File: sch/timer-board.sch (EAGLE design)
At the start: 33 parts, among them IC1 ATMEGA328P

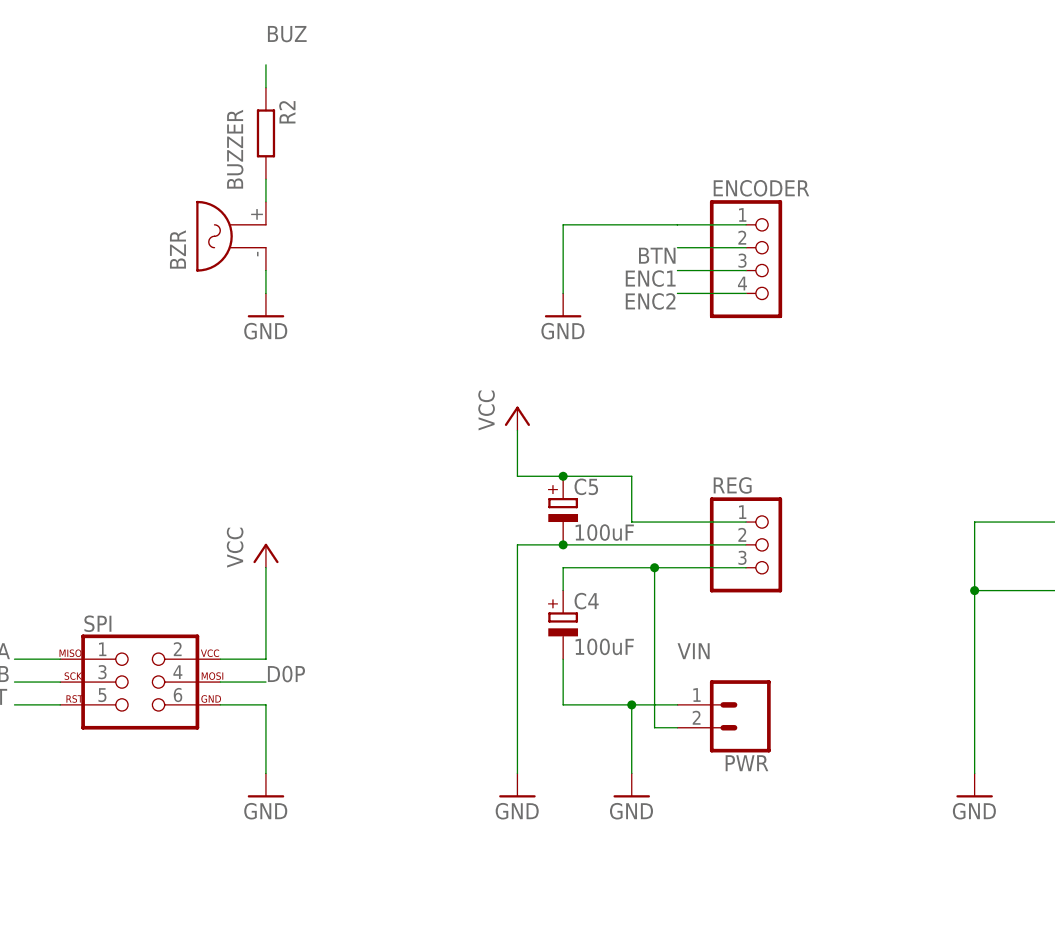
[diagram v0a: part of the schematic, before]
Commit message: Updated schematic to use new parts Added PCB first version
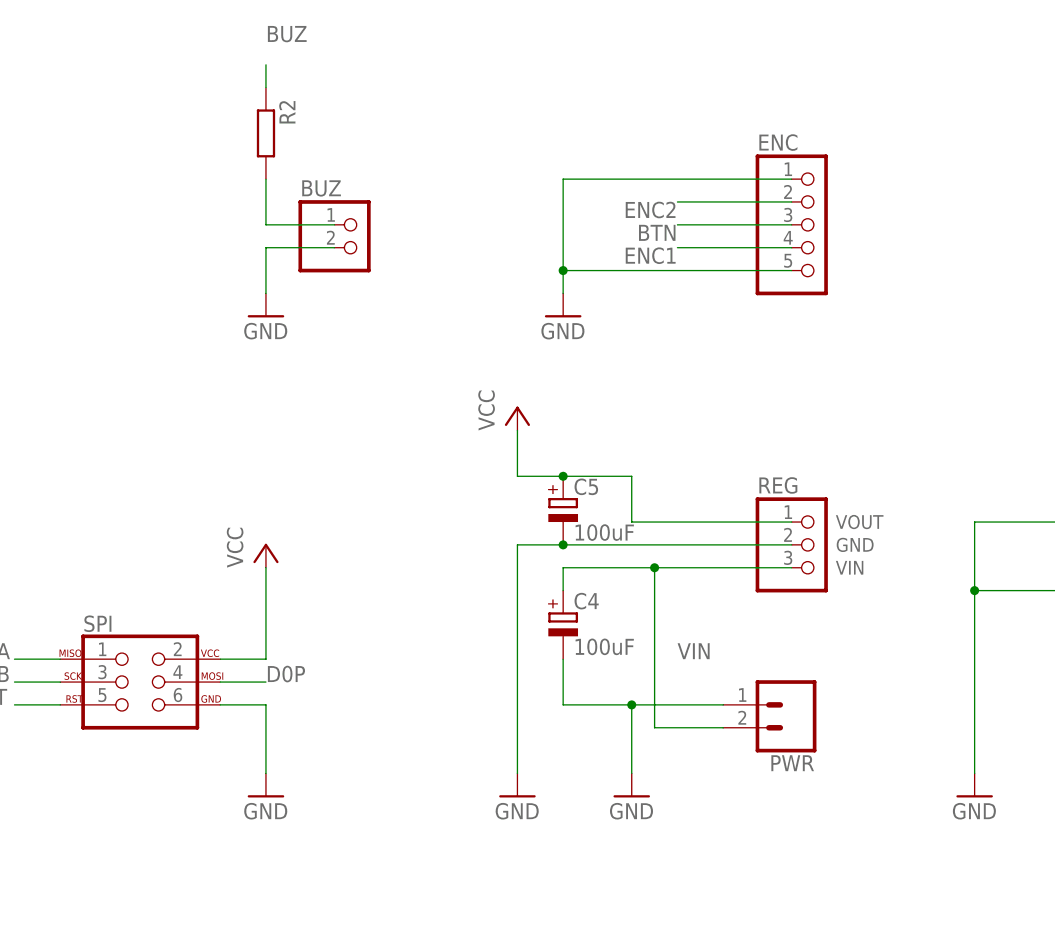
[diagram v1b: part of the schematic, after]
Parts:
- removed BZR: BUZZER, parts:BUZZER
- removed ENCODER: (no value), pinhead:PINHD-1X4/90
- added BUZ: (no value), pinhead:PINHD-1X2/90
- added ENC: CONN_1X5, parts:CONN_1X5
- C1, C2, C3, C6: device resistor:C-EU050-025X075 -> rcl:C-EU025-025X050
- REG: value (none) -> VREG_STEP_UP; device pinhead:PINHD-1X3/90 -> parts:VREG_STEP_UP
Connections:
- net BTN: now also ENC.3; no longer ENCODER.2
- net ENC1: now also ENC.4; no longer ENCODER.3
- net ENC2: now also ENC.2; no longer ENCODER.4
- net GND: now also BUZ.2, ENC.1, ENC.5, REG.GND; no longer BZR.1, ENCODER.1, REG.2
- net N$8: now also BUZ.1; no longer BZR.2
- net VCC: now also REG.VOUT; no longer REG.1
- net VIN: now also REG.VIN; no longer REG.3
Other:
- moved on the sheet: PWR

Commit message: PCB : Added some logos
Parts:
- added LOGO1: OSHW-LOGOL-COPPER, SparkFun-Aesthetics:OSHW-LOGOL-COPPER
- added U$1: DOG_LOGO, parts:DOG_LOGO
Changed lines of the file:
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@@
 <part name="ENC" library="parts" deviceset="CONN_1X5" device="" value=""/>
 <part name="REG" library="parts" deviceset="VREG_STEP_UP" device="" value=""/>
+<part name="LOGO1" library="SparkFun-Aesthetics" library_urn="urn:adsk.eagle:library:507" deviceset="OSHW-LOGO" device="L-COPPER" package3d_urn="urn:adsk.eagle:package:37117/1"/>
+<part name="U$1" library="parts" deviceset="DOG_LOGO" device=""/>
 </parts>
 <sheets>
@@
 <instance part="ENC" gate="G$1" x="-73.66" y="35.56"/>
 <instance part="REG" gate="G$1" x="-73.66" y="-2.54"/>
+<instance part="LOGO1" gate="G$1" x="-88.9" y="73.66"/>
+<instance part="U$1" gate="G$1" x="-71.12" y="66.04"/>
 </instances>
 <busses>

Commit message: PCB : Fixed resistor label
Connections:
- net BUZ: now also R2.2; no longer R2.1
- net N$8: now also R2.1; no longer R2.2
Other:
- moved on the sheet: R2
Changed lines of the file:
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@@
 <part name="GND1" library="supply1" library_urn="urn:adsk.eagle:library:371" deviceset="GND" device=""/>
 <part name="R1" library="rcl" library_urn="urn:adsk.eagle:library:334" deviceset="R-EU_" device="0207/10" package3d_urn="urn:adsk.eagle:package:23491/1" value="10k"/>
-<part name="R2" library="rcl" library_urn="urn:adsk.eagle:library:334" deviceset="R-EU_" device="0207/10" package3d_urn="urn:adsk.eagle:package:23491/1"/>
 <part name="P+1" library="supply1" library_urn="urn:adsk.eagle:library:371" deviceset="VCC" device=""/>
 <part name="GND10" library="supply1" library_urn="urn:adsk.eagle:library:371" deviceset="GND" device=""/>
@@
 <part name="LOGO1" library="SparkFun-Aesthetics" library_urn="urn:adsk.eagle:library:507" deviceset="OSHW-LOGO" device="L-COPPER" package3d_urn="urn:adsk.eagle:package:37117/1"/>
 <part name="U$1" library="parts" deviceset="DOG_LOGO" device=""/>
+<part name="R2" library="rcl" library_urn="urn:adsk.eagle:library:334" deviceset="R-EU_" device="0207/10" package3d_urn="urn:adsk.eagle:package:23491/1"/>
 </parts>
 <sheets>
@@
 <instance part="GND1" gate="1" x="-134.62" y="22.86"/>
 <instance part="R1" gate="G$1" x="-25.4" y="22.86" rot="R90"/>
-<instance part="R2" gate="G$1" x="-134.62" y="43.18" rot="R270"/>
 <instance part="P+1" gate="VCC" x="-106.68" y="12.7"/>
 <instance part="GND10" gate="1" x="-106.68" y="-30.48"/>
@@
 <instance part="LOGO1" gate="G$1" x="-88.9" y="73.66"/>
 <instance part="U$1" gate="G$1" x="-71.12" y="66.04"/>
+<instance part="R2" gate="G$1" x="-134.62" y="43.18" rot="R90"/>
 </instances>
 <busses>
@@
 <wire x1="-134.62" y1="50.8" x2="-134.62" y2="48.26" width="0.1524" layer="91"/>
 <label x="-134.62" y="53.34" size="1.778" layer="95"/>
-<pinref part="R2" gate="G$1" pin="1"/>
+<pinref part="R2" gate="G$1" pin="2"/>
 </segment>
 </net>
@@
 <net name="N$8" class="0">
 <segment>
-<pinref part="R2" gate="G$1" pin="2"/>
 <pinref part="BUZ" gate="G$1" pin="1"/>
 <wire x1="-127" y1="33.02" x2="-134.62" y2="33.02" width="0.1524" layer="91"/>
 <wire x1="-134.62" y1="33.02" x2="-134.62" y2="38.1" width="0.1524" layer="91"/>
-</segment>
-</net>
+<pinref part="R2" gate="G$1" pin="1"/>
+</segment>
+</net>

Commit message: PCB : Updated dog logo
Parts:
- U$1: value DOG_LOGO -> LOGO_DOG; device parts:DOG_LOGO -> parts:LOGO_DOG
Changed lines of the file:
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@@
 <part name="REG" library="parts" deviceset="VREG_STEP_UP" device="" value=""/>
 <part name="LOGO1" library="SparkFun-Aesthetics" library_urn="urn:adsk.eagle:library:507" deviceset="OSHW-LOGO" device="L-COPPER" package3d_urn="urn:adsk.eagle:package:37117/1"/>
-<part name="U$1" library="parts" deviceset="DOG_LOGO" device=""/>
+<part name="U$1" library="parts" deviceset="LOGO_DOG" device=""/>
 <part name="R2" library="rcl" library_urn="urn:adsk.eagle:library:334" deviceset="R-EU_" device="0207/10" package3d_urn="urn:adsk.eagle:package:23491/1"/>
 </parts>

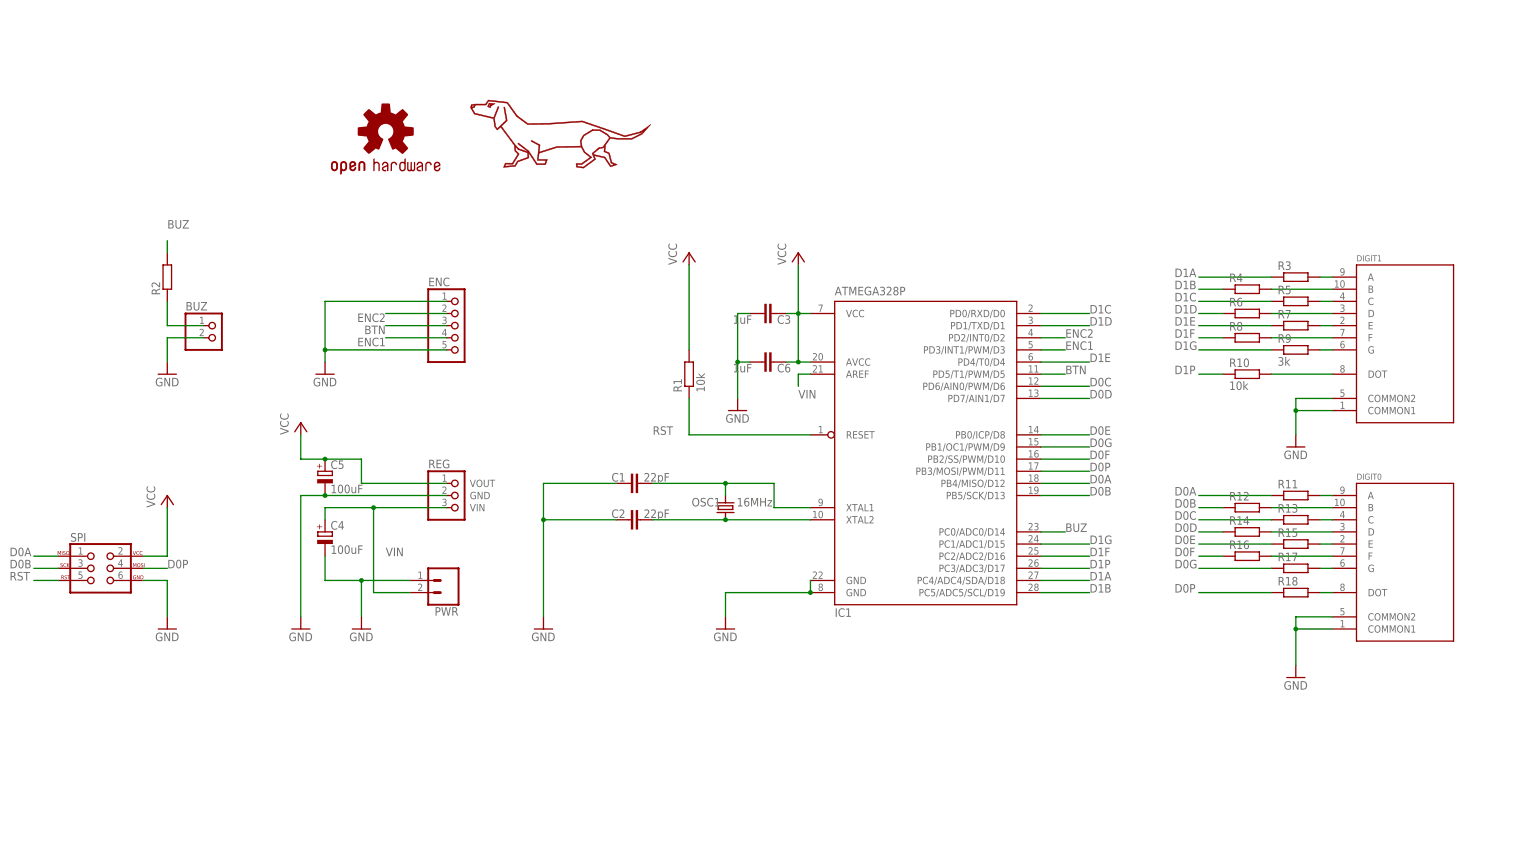
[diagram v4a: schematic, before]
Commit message: SCH : Added frame
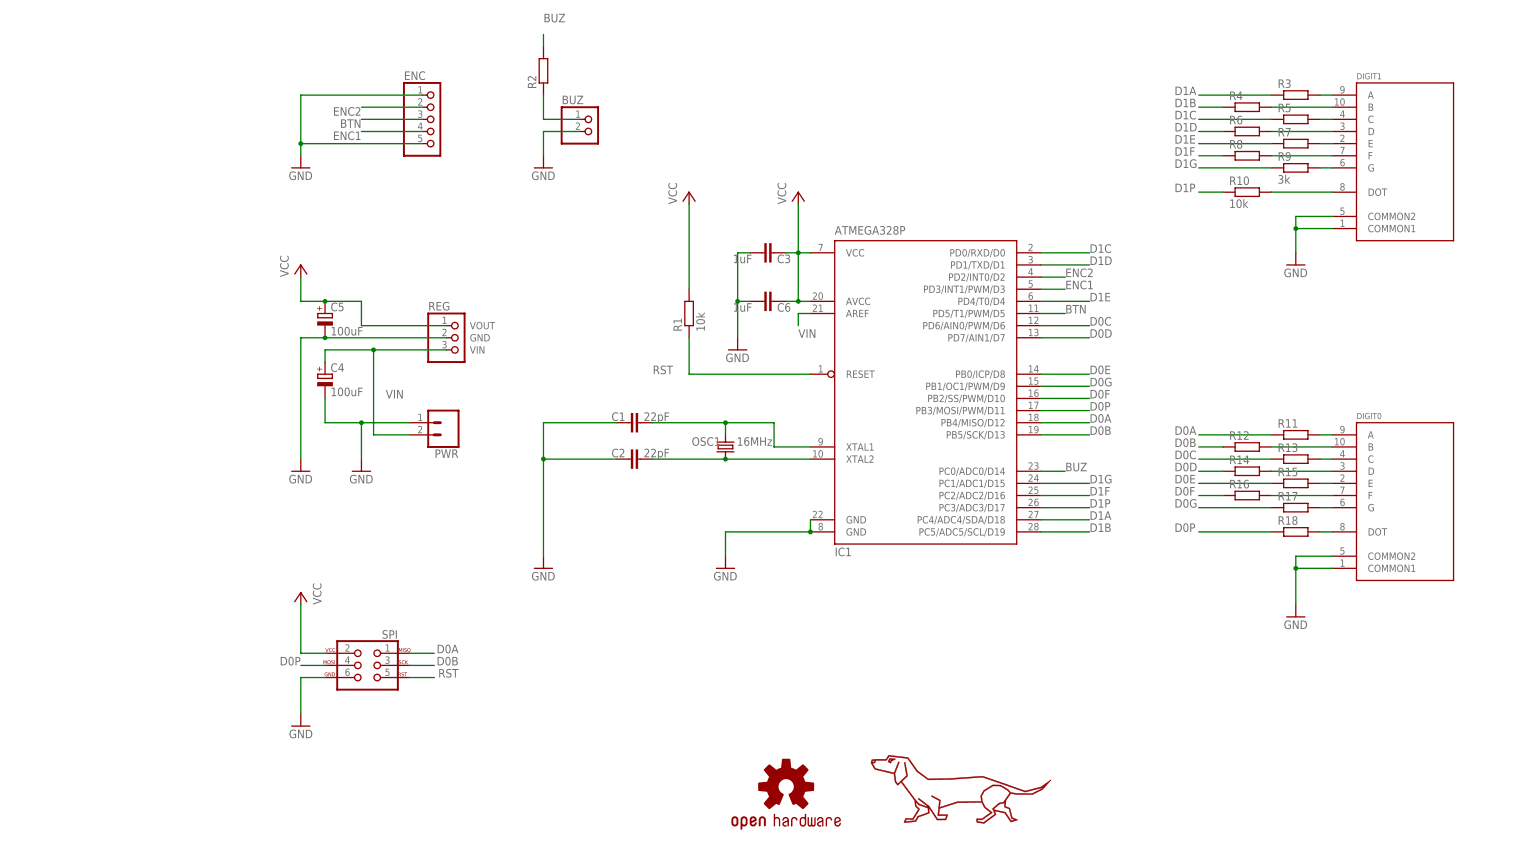
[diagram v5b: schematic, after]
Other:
- moved on the sheet: BUZ, C1, C2, C3, C4, C5, C6, DIGIT0, DIGIT1, ENC, IC1, OSC1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

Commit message: feat: updated board to smaller layout
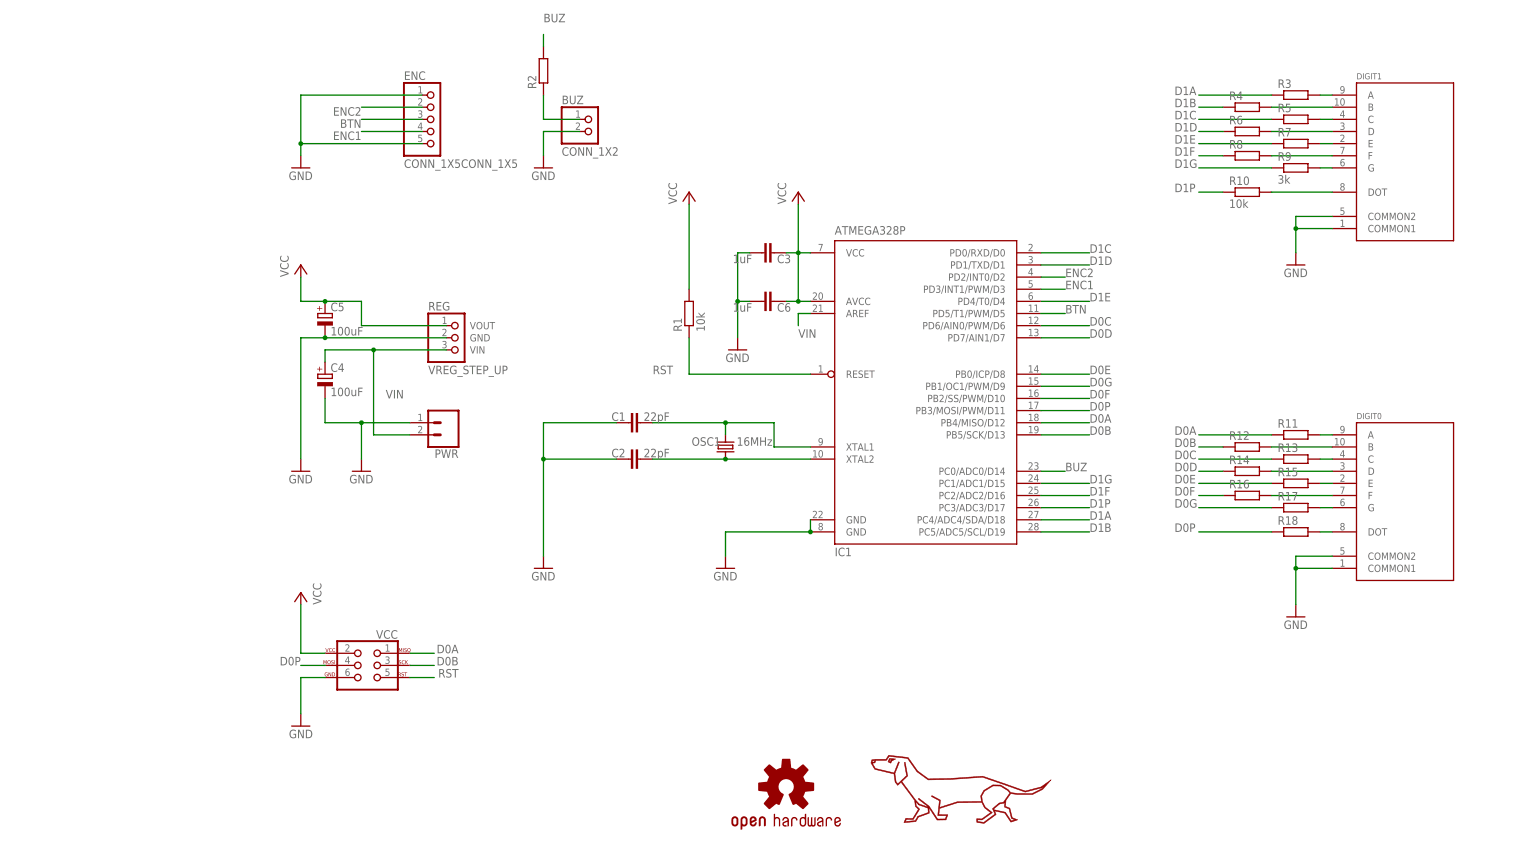
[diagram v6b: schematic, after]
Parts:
- BUZ: value (none) -> CONN_1X2; device pinhead:PINHD-1X2/90 -> parts:CONN_1X2
- ENC: value CONN_1X5 -> CONN_1X5CONN_1X5; device parts:CONN_1X5 -> parts:CONN_1X5CONN_1X5
- renumbered SPI to VCC
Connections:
- net GND: now also BUZ.1; no longer BUZ.2
- net N$8: now also BUZ.0; no longer BUZ.1

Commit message: refactoring: reworked routing
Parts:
- removed C5: 100uF, rcl:CPOL-EUE2.5-6
- removed REG: VREG_STEP_UP, parts:VREG_STEP_UP
- added R19: (no value), rcl:R-EU_0207/10
- added T1: 2N3904, transistor:2N3904
- BUZ: value CONN_1X2 -> BUZZER2_IN_1; device parts:CONN_1X2 -> parts:BUZZER2_IN_1
- C4: value 100uF -> 10uF
- LOGO1: value OSHW-LOGOL-COPPER -> OSHW-LOGOL; device SparkFun-Aesthetics:OSHW-LOGOL-COPPER -> SparkFun-Aesthetics:OSHW-LOGOL
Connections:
- removed net VIN: C4.+, IC1.AREF, PWR.2, REG.VIN
- new net N$10: R2.1, T1.B
- net BTN: now also ENC.4; no longer ENC.3
- net BUZ: now also IC1.PB1/OC1/PWM/D9; no longer IC1.PC0/ADC0/D14
- net D0C: now also IC1.PB0/ICP/D8; no longer IC1.PD6/AIN0/PWM/D6
- net D0E: now also IC1.PD6/AIN0/PWM/D6; no longer IC1.PB0/ICP/D8
- net D0G: now also IC1.PC0/ADC0/D14; no longer IC1.PB1/OC1/PWM/D9
- net ENC1: now also ENC.3; no longer ENC.4
- net GND: now also R19.1; no longer C5.-, REG.GND
- net N$8: now also BUZ.2, R19.2, T1.E; no longer BUZ.0, R2.1
- net VCC: now also C4.+, PWR.2, T1.C; no longer C5.+, REG.VOUT
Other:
- moved on the sheet: BUZ, C1, C2, C3, C4, C6, DIGIT0, DIGIT1, ENC, IC1, OSC1, PWR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

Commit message: refactoring: finalized routing
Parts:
- removed C6: 1uF, rcl:C-EU025-025X050
- removed IC1: ATMEGA328P, parts:ATMEGA328P
- added C5: 10uF, rcl:CPOL-EUE2.5-6
- added J1: (no value), SparkFun-Connectors:CONN_02LOCK
- added R20: (no value), rcl:R-TRIMM3296W
- added U2: 328P, SparkFun-IC-Microcontroller:ATMEGA328P_PDIP
- BUZ: value BUZZER2_IN_1 -> CONN_1X2JST; device parts:BUZZER2_IN_1 -> parts:CONN_1X2JST
- C1, C2: device rcl:C-EU025-025X050 -> rcl:C-EU050-024X044
- C3: value 1uF -> 0.1uF; device rcl:C-EU025-025X050 -> rcl:C-EU050-024X044
- C4: value 10uF -> 0.1uF; device rcl:CPOL-EUE2.5-6 -> rcl:C-EU050-024X044
- DIGIT0, DIGIT1: value 7-SEGMENT-DISPLAY -> 7_SEGMENT_DISPLAY; device parts:7-SEGMENT-DISPLAY -> parts:7_SEGMENT_DISPLAY
- ENC: value CONN_1X5CONN_1X5 -> CONN_1X5; device parts:CONN_1X5CONN_1X5 -> parts:CONN_1X5JST
- PWR: value (none) -> 5V; device SparkFun-Connectors:CONN_02JST-PTH-2 -> parts:CONN_1X2JST
- R10: value 10k -> (none)
- R9: value 3k -> (none)
- renumbered VCC to PROG
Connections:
- removed net N$8: BUZ.2, R19.2, T1.E
- new net N$11: C5.+, J1.2, PWR.2
- new net N$12: R20.A, T1.E
- new net N$21: BUZ.2, R19.2, R20.S
- net BTN: now also U2.PD5(T1); no longer IC1.PD5/T1/PWM/D5
- net BUZ: now also U2.PB1(OC1A); no longer IC1.PB1/OC1/PWM/D9
- net D0A: now also U2.PB4(MISO); no longer IC1.PB4/MISO/D12
- net D0B: now also U2.PB5(SCK); no longer IC1.PB5/SCK/D13
- net D0C: now also U2.PB0(ICP); no longer IC1.PB0/ICP/D8
- net D0D: now also U2.PD7(AIN1); no longer IC1.PD7/AIN1/D7
- net D0E: now also U2.PD6(AIN0); no longer IC1.PD6/AIN0/PWM/D6
- net D0F: now also U2.PB2(SS/OC1B); no longer IC1.PB2/SS/PWM/D10
- net D0G: now also U2.PC0(ADC0); no longer IC1.PC0/ADC0/D14
- net D0P: now also U2.PB3(MOSI/OC2); no longer IC1.PB3/MOSI/PWM/D11
- net D1A: now also U2.PC4(ADC4/SDA); no longer IC1.PC4/ADC4/SDA/D18
- net D1B: now also U2.PC5(ADC5/SCL); no longer IC1.PC5/ADC5/SCL/D19
- net D1C: now also U2.PD0(RXD); no longer IC1.PD0/RXD/D0
- net D1D: now also U2.PD1(TXD); no longer IC1.PD1/TXD/D1
- net D1E: now also U2.PD4(XCK/T0); no longer IC1.PD4/T0/D4
- net D1F: now also U2.PC2(ADC2); no longer IC1.PC2/ADC2/D16
- net D1G: now also U2.PC1(ADC1); no longer IC1.PC1/ADC1/D15
- net D1P: now also U2.PC3(ADC3); no longer IC1.PC3/ADC3/D17
- net ENC1: now also U2.PD3(INT1); no longer IC1.PD3/INT1/PWM/D3
- net ENC2: now also U2.PD2(INT0); no longer IC1.PD2/INT0/D2
- net GND: now also C4.2, C5.-, U2.GND@1, U2.GND@2; no longer C4.-, C6.2, IC1.GND@1, IC1.GND@2
- net RST: now also U2.PC6(/RESET); no longer IC1.RESET
- net VCC: now also C4.1, J1.1, U2.AVCC, U2.VCC; no longer C4.+, C6.1, IC1.AVCC, IC1.VCC@1, PWR.2
- net XTAL1: now also U2.PB6(XTAL1/TOSC1); no longer IC1.XTAL1
- net XTAL2: now also U2.PB7(XTAL2/TOSC2); no longer IC1.XTAL2
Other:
- moved on the sheet: BUZ, C1, C2, C3, OSC1, PWR, R1, R19, R2, T1
